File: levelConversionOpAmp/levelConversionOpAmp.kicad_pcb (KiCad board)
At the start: 2 copper layers, 21 parts, among them J1 IN, J2 OUT, Q1 PN2222A, Q2 PN2222A, U1 TL082

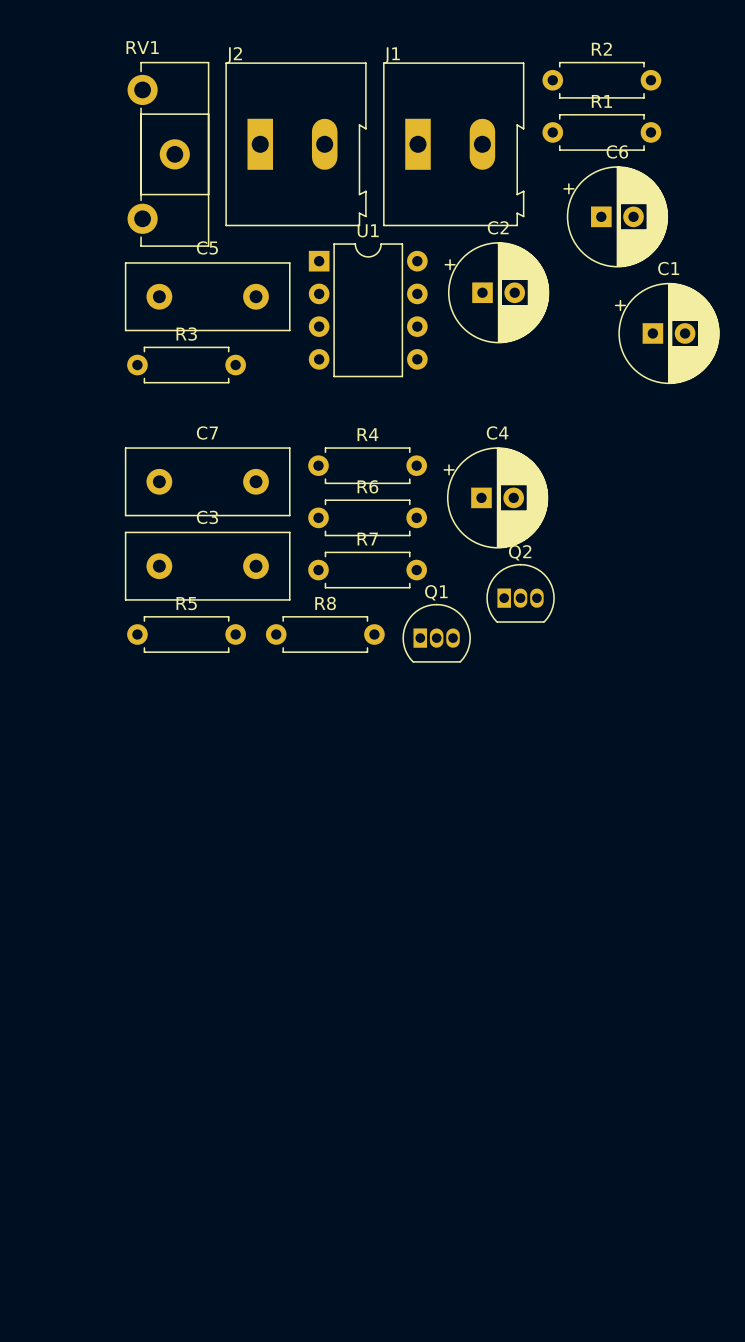
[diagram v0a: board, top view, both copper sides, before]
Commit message: Placement des composantes sur plaque perforee
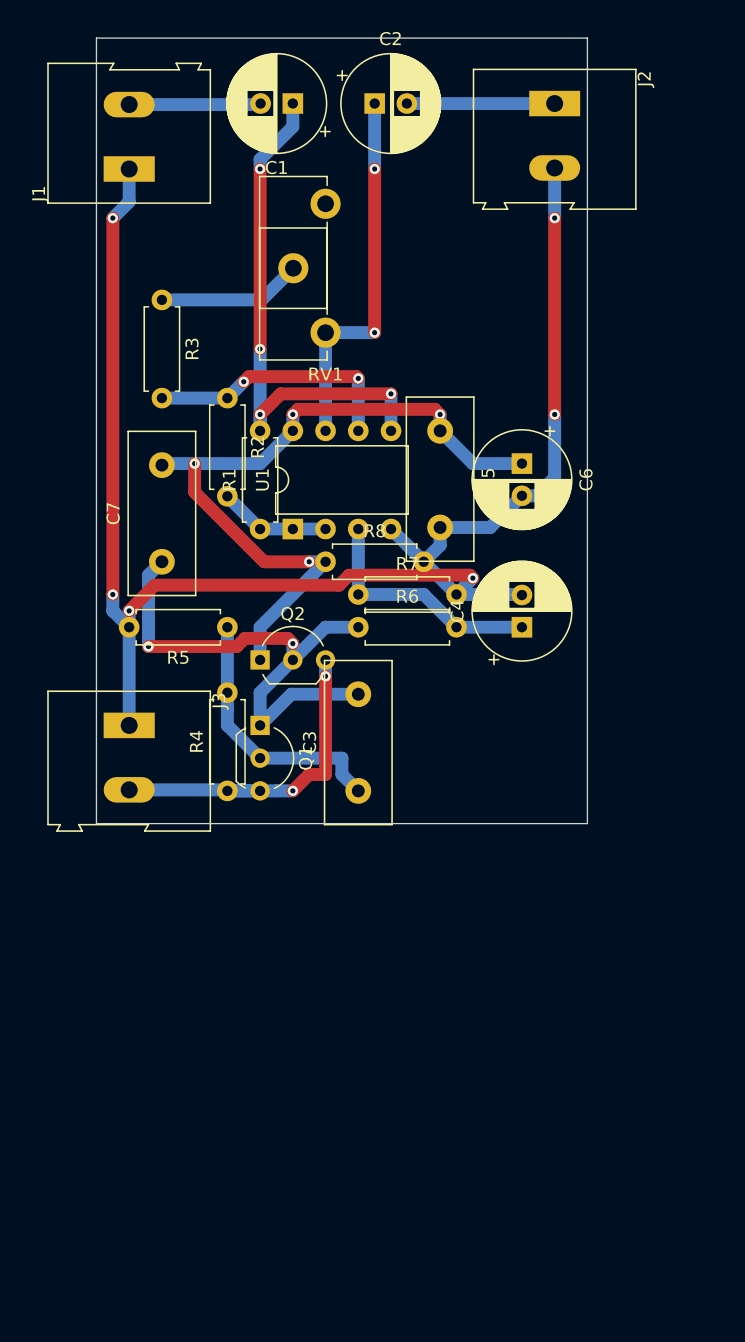
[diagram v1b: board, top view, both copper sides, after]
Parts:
- added J3: POW, TerminalBlock:TerminalBlock_Altech_AK300-2_P5.00mm, F.Cu at (129.5, 101.6)
- Q1, Q2: footprint Package_TO_SOT_THT:TO-92_Inline -> Package_TO_SOT_THT:TO-92_Inline_Wide
- moved R1 38.2 mm to (139.7, 86.4), turned to 90 degrees
- moved R2 35.3 mm to (137.2, 76.2), turned to 270 degrees
- moved C1 33.2 mm to (142.2, 53.3), turned to 180 degrees
- moved R4 26.2 mm to (137.2, 106.7), turned to 90 degrees
- moved C5 24.1 mm to (153.7, 78.7), turned to 270 degrees
- moved RV1 23.6 mm to (144.8, 71.1), turned to 180 degrees
- moved C3 23.3 mm to (147.3, 106.7), turned to 90 degrees
- moved J2 23.1 mm to (162.6, 53.3), turned to 270 degrees
- moved J1 22.5 mm to (129.5, 58.4), turned to 90 degrees
- moved U1 20.9 mm to (142.2, 86.4), turned to 90 degrees
- moved C6 20.1 mm to (160.0, 81.3), turned to 270 degrees
- moved Q2 19.5 mm to (139.7, 96.5)
- moved C2 16.9 mm to (148.6, 53.3)
- moved Q1 14.2 mm to (139.7, 101.6), turned to 270 degrees
- moved C4 10.5 mm to (160.0, 94.0), turned to 90 degrees
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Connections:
- J2 pad 1: GND -> SIGOUT
- J2 pad 2: SIGOUT -> GND
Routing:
- net GND: track 0.00 -> 125.2 mm, vias 0 -> 6
- net V+: track 0.00 -> 57.3 mm, vias 0 -> 4
- net Net-(C1-Pad1): track 0.00 -> 41.4 mm, vias 0 -> 4
- net Net-(C3-Pad2): track 0.00 -> 40.8 mm, vias 0 -> 2
- net Net-(C2-Pad1): track 0.00 -> 29.2 mm, vias 0 -> 2
- net +48V: track 0.00 -> 27.2 mm, vias 0 -> 2
- net Net-(C3-Pad1): track 0.00 -> 20.6 mm
- net Net-(R2-Pad1): track 0.00 -> 20.1 mm, vias 0 -> 2
- net Net-(C4-Pad1): track 0.00 -> 18.8 mm
- net SIGOUT: track 0.00 -> 11.5 mm
- net Net-(R3-Pad1): track 0.00 -> 11.2 mm
- net SIGIN: track 0.00 -> 10.2 mm
- net VREF: track 0.00 -> 8.67 mm
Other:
- board outline added: 38.1 x 61 mm

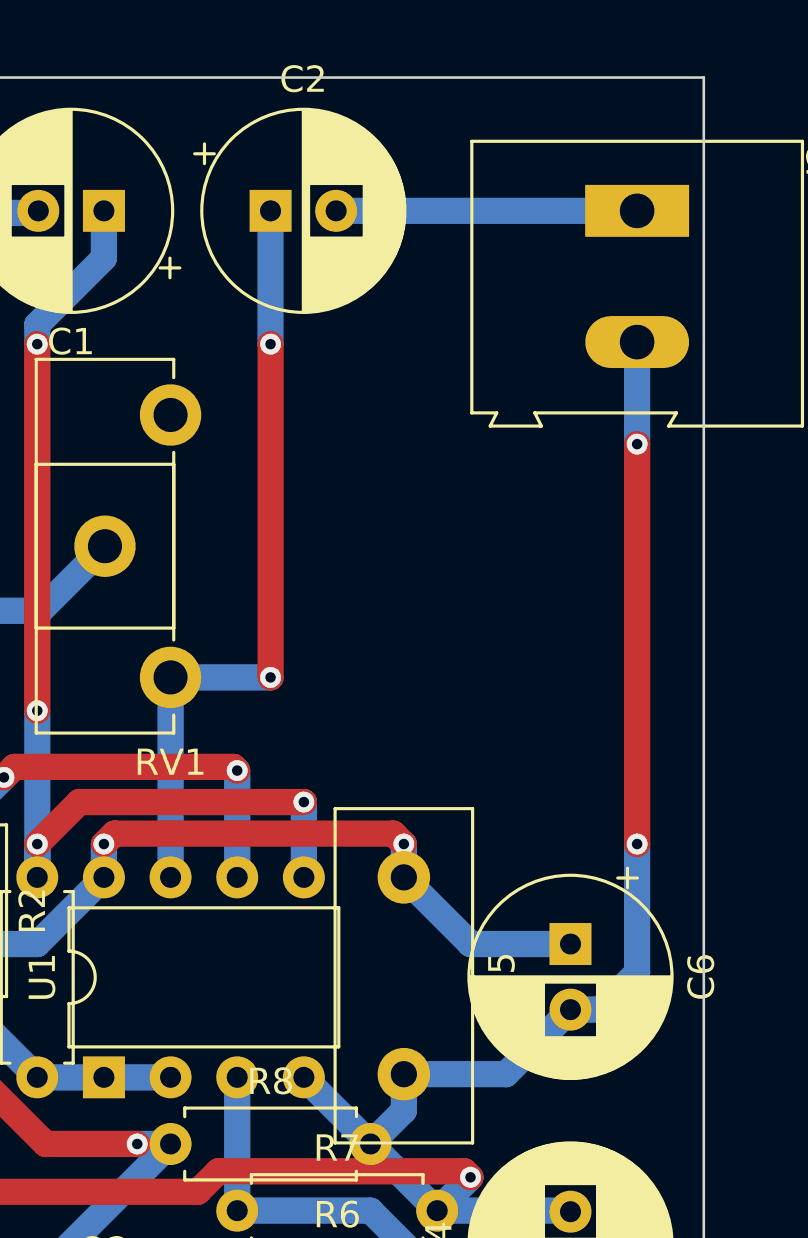
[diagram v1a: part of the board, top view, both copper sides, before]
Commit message: Changed layout a little. Added ground bias resistor at output to quickly set output DC level even when plugged into a high impedance load
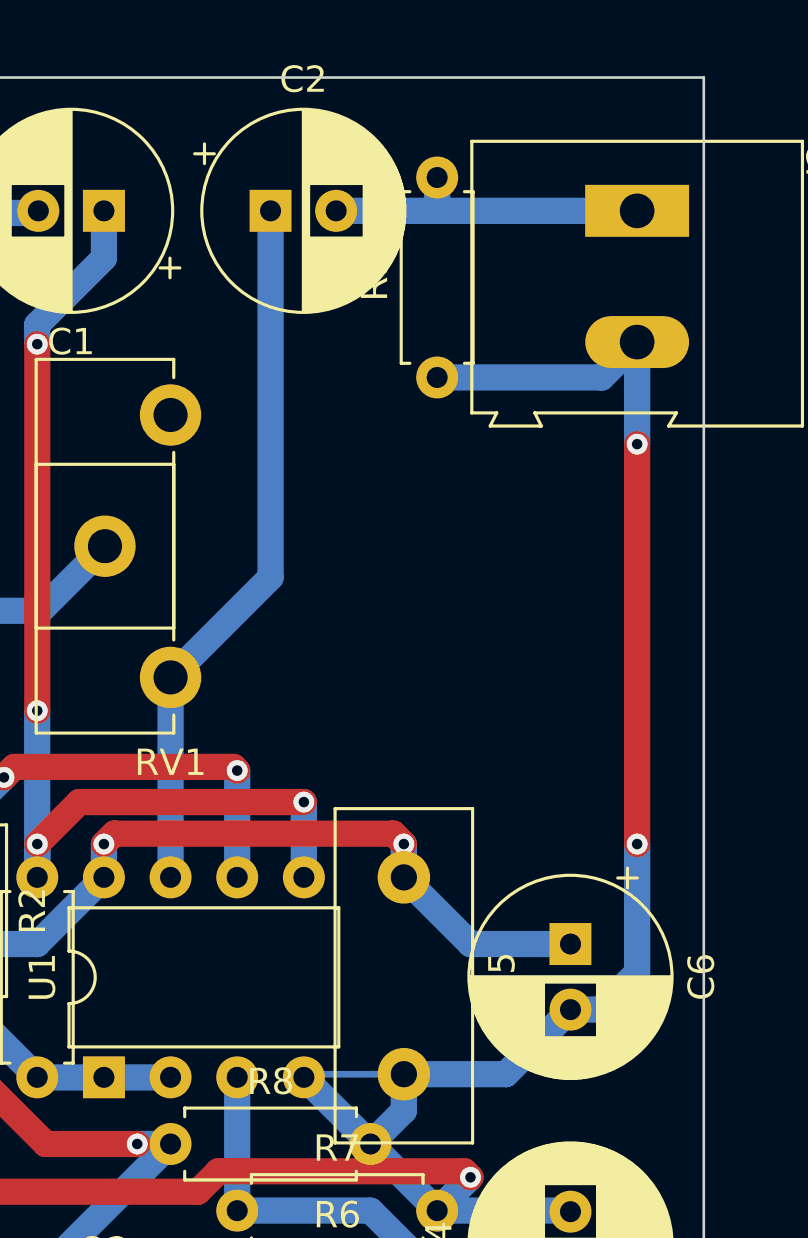
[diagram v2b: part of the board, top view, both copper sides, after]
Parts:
- added R9: 4k7, Resistor_THT:R_Axial_DIN0207_L6.3mm_D2.5mm_P7.62mm_Horizontal, F.Cu at (154.9, 59.7)
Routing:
- net GND: track 125.2 -> 137.2 mm
- net Net-(C2-Pad1): track 29.2 -> 27.0 mm, vias 2 -> 0
- net SIGOUT: track 11.5 -> 12.7 mm
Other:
- net class Default: via_dia 0.8 -> 0.5; via_drill 0.4 -> 0.3
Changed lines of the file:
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@@
     (thickness 1.6)
     (drawings 4)
-    (tracks 125)
+    (tracks 128)
     (zones 0)
-    (modules 22)
+    (modules 23)
     (nets 14)
   )
@@
   (setup
     (last_trace_width 1)
+    (user_trace_width 0.5)
     (user_trace_width 1)
     (trace_clearance 0.2)
@@
     (zone_45_only no)
     (trace_min 0.2)
-    (via_size 0.8)
-    (via_drill 0.4)
+    (via_size 0.5)
+    (via_drill 0.3)
     (via_min_size 0.4)
     (via_min_drill 0.3)
@@
     (clearance 0.2)
     (trace_width 0.25)
-    (via_dia 0.8)
-    (via_drill 0.4)
+    (via_dia 0.5)
+    (via_drill 0.3)
     (uvia_dia 0.3)
     (uvia_drill 0.1)
@@
     (add_net V+)
     (add_net VREF)
+  )
+  (module Resistor_THT:R_Axial_DIN0207_L6.3mm_D2.5mm_P7.62mm_Horizontal (layer F.Cu)
+    (at 154.94 59.69 90)
+    (descr "Resistor, Axial_DIN0207 series, Axial, Horizontal, pin pitch=7.62mm, 0.25W = 1/4W, length*diameter=6.3*2.5mm^2, http://cdn-reichelt.de/documents/datenblatt/B400/1_4W%23YAG.pdf")
+    (tags "Resistor Axial_DIN0207 series Axial Horizontal pin pitch 7.62mm 0.25W = 1/4W length 6.3mm diameter 2.5mm")
+    (fp_text reference R9 (at 3.81 -2.37 90) (layer F.SilkS)
+      (effects (font (size 1 1) (thickness 0.15)))
+    )
+    (fp_text value 4k7 (at 3.81 2.37 90) (layer F.Fab)
+      (effects (font (size 1 1) (thickness 0.15)))
+    )
+    (fp_text user %R (at 3.81 0 90) (layer F.Fab)
+      (effects (font (size 1 1) (thickness 0.15)))
+    )
+    (fp_line (start 8.67 -1.5) (end -1.05 -1.5) (layer F.CrtYd) (width 0.05))
+    (fp_line (start 8.67 1.5) (end 8.67 -1.5) (layer F.CrtYd) (width 0.05))
+    (fp_line (start -1.05 1.5) (end 8.67 1.5) (layer F.CrtYd) (width 0.05))
+    (fp_line (start -1.05 -1.5) (end -1.05 1.5) (layer F.CrtYd) (width 0.05))
+    (fp_line (start 7.08 1.37) (end 7.08 1.04) (layer F.SilkS) (width 0.12))
+    (fp_line (start 0.54 1.37) (end 7.08 1.37) (layer F.SilkS) (width 0.12))
+    (fp_line (start 0.54 1.04) (end 0.54 1.37) (layer F.SilkS) (width 0.12))
+    (fp_line (start 7.08 -1.37) (end 7.08 -1.04) (layer F.SilkS) (width 0.12))
+    (fp_line (start 0.54 -1.37) (end 7.08 -1.37) (layer F.SilkS) (width 0.12))
+    (fp_line (start 0.54 -1.04) (end 0.54 -1.37) (layer F.SilkS) (width 0.12))
+    (fp_line (start 7.62 0) (end 6.96 0) (layer F.Fab) (width 0.1))
+    (fp_line (start 0 0) (end 0.66 0) (layer F.Fab) (width 0.1))
+    (fp_line (start 6.96 -1.25) (end 0.66 -1.25) (layer F.Fab) (width 0.1))
+    (fp_line (start 6.96 1.25) (end 6.96 -1.25) (layer F.Fab) (width 0.1))
+    (fp_line (start 0.66 1.25) (end 6.96 1.25) (layer F.Fab) (width 0.1))
+    (fp_line (start 0.66 -1.25) (end 0.66 1.25) (layer F.Fab) (width 0.1))
+    (pad 2 thru_hole oval (at 7.62 0 90) (size 1.6 1.6) (drill 0.8) (layers *.Cu *.Mask)
+      (net 3 SIGOUT))
+    (pad 1 thru_hole circle (at 0 0 90) (size 1.6 1.6) (drill 0.8) (layers *.Cu *.Mask)
+      (net 7 GND))
+    (model ${KISYS3DMOD}/Resistor_THT.3dshapes/R_Axial_DIN0207_L6.3mm_D2.5mm_P7.62mm_Horizontal.wrl
+      (at (xyz 0 0 0))
+      (scale (xyz 1 1 1))
+      (rotate (xyz 0 0 0))
+    )
   )
   (module Potentiometer_THT:Potentiometer_ACP_CA14-H2,5_Horizontal (layer F.Cu)
@@
   (segment (start 139.66 53.42) (end 139.74 53.34) (width 1) (layer B.Cu) (net 1))
   (segment (start 129.54 53.42) (end 139.66 53.42) (width 1) (layer B.Cu) (net 1))
-  (via (at 139.7 77.47) (size 0.8) (drill 0.4) (layers F.Cu B.Cu) (net 2))
-  (segment (start 139.7 78.74) (end 139.7 77.47) (width 1) (layer B.Cu) (net 2))
-  (segment (start 141.300009 75.869991) (end 149.86 75.869991) (width 1) (layer F.Cu) (net 2))
-  (segment (start 139.7 77.47) (end 141.300009 75.869991) (width 1) (layer F.Cu) (net 2))
-  (via (at 149.86 75.869991) (size 0.8) (drill 0.4) (layers F.Cu B.Cu) (net 2))
-  (segment (start 149.86 75.869991) (end 149.86 78.74) (width 1) (layer B.Cu) (net 2))
   (segment (start 142.24 55.14) (end 139.7 57.68) (width 1) (layer B.Cu) (net 2))
   (segment (start 142.24 53.34) (end 142.24 55.14) (width 1) (layer B.Cu) (net 2))
@@
   (via (at 139.7 72.39) (size 0.8) (drill 0.4) (layers F.Cu B.Cu) (net 2))
   (segment (start 139.7 58.42) (end 139.7 72.39) (width 1) (layer F.Cu) (net 2))
+  (segment (start 139.7 78.74) (end 139.7 77.47) (width 1) (layer B.Cu) (net 2))
   (segment (start 139.7 72.39) (end 139.7 78.74) (width 1) (layer B.Cu) (net 2))
-  (segment (start 151.09 53.34) (end 162.56 53.34) (width 1) (layer B.Cu) (net 3))
-  (via (at 148.59 71.12) (size 0.8) (drill 0.4) (layers F.Cu B.Cu) (net 4))
-  (via (at 148.59 58.42) (size 0.8) (drill 0.4) (layers F.Cu B.Cu) (net 4))
-  (segment (start 148.59 71.12) (end 148.59 58.42) (width 1) (layer F.Cu) (net 4))
-  (segment (start 148.59 58.42) (end 148.59 53.34) (width 1) (layer B.Cu) (net 4))
-  (segment (start 144.78 71.12) (end 148.59 71.12) (width 1) (layer B.Cu) (net 4))
+  (segment (start 149.86 75.869991) (end 149.86 78.74) (width 1) (layer B.Cu) (net 2))
+  (via (at 149.86 75.869991) (size 0.8) (drill 0.4) (layers F.Cu B.Cu) (net 2))
+  (segment (start 141.300009 75.869991) (end 149.86 75.869991) (width 1) (layer F.Cu) (net 2))
+  (via (at 139.7 77.47) (size 0.8) (drill 0.4) (layers F.Cu B.Cu) (net 2))
+  (segment (start 139.7 77.47) (end 141.300009 75.869991) (width 1) (layer F.Cu) (net 2))
+  (segment (start 154.94 52.07) (end 154.94 53.34) (width 1) (layer B.Cu) (net 3))
+  (segment (start 154.94 53.34) (end 162.56 53.34) (width 1) (layer B.Cu) (net 3))
+  (segment (start 151.09 53.34) (end 154.94 53.34) (width 1) (layer B.Cu) (net 3))
   (segment (start 144.78 71.12) (end 144.78 78.74) (width 1) (layer B.Cu) (net 4))
+  (segment (start 148.59 67.31) (end 144.78 71.12) (width 1) (layer B.Cu) (net 4))
+  (segment (start 148.59 53.34) (end 148.59 67.31) (width 1) (layer B.Cu) (net 4))
   (segment (start 144.78 93.98) (end 142.24 96.52) (width 1) (layer B.Cu) (net 5))
   (segment (start 147.32 93.98) (end 144.78 93.98) (width 1) (layer B.Cu) (net 5))
@@
   (segment (start 162.56 82.37137) (end 161.15137 83.78) (width 1) (layer B.Cu) (net 7))
   (segment (start 162.56 77.47) (end 162.56 82.37137) (width 1) (layer B.Cu) (net 7))
+  (segment (start 149.98 86.24) (end 149.86 86.36) (width 0.25) (layer B.Cu) (net 7))
+  (segment (start 153.67 86.24) (end 149.98 86.24) (width 0.25) (layer B.Cu) (net 7))
+  (segment (start 161.21 59.69) (end 162.56 58.34) (width 1) (layer B.Cu) (net 7))
+  (segment (start 154.94 59.69) (end 161.21 59.69) (width 1) (layer B.Cu) (net 7))
   (segment (start 152.4 91.44) (end 154.94 93.98) (width 1) (layer B.Cu) (net 8))
   (segment (start 147.32 91.44) (end 152.4 91.44) (width 1) (layer B.Cu) (net 8))
@@
   (segment (start 132.2 81.28) (end 132.08 81.4) (width 1) (layer B.Cu) (net 9))
   (segment (start 134.62 81.28) (end 132.2 81.28) (width 1) (layer B.Cu) (net 9))
-  (segment (start 139.7 81.28) (end 142.24 78.74) (width 1) (layer B.Cu) (net 9))
-  (segment (start 134.62 81.28) (end 139.7 81.28) (width 1) (layer B.Cu) (net 9))
   (segment (start 156.21 81.28) (end 153.67 78.74) (width 1) (layer B.Cu) (net 9))
   (segment (start 160.02 81.28) (end 156.21 81.28) (width 1) (layer B.Cu) (net 9))
@@
   (segment (start 153.67 77.47) (end 153.270001 77.070001) (width 1) (layer F.Cu) (net 9))
   (segment (start 142.24 77.47) (end 142.24 78.74) (width 1) (layer B.Cu) (net 9))
+  (segment (start 139.7 81.28) (end 142.24 78.74) (width 1) (layer B.Cu) (net 9))
+  (segment (start 134.62 81.28) (end 139.7 81.28) (width 1) (layer B.Cu) (net 9))
   (segment (start 137.08 106.6) (end 137.16 106.68) (width 1) (layer B.Cu) (net 10))
   (segment (start 129.54 106.6) (end 137.08 106.6) (width 1) (layer B.Cu) (net 10))
@@
   (segment (start 142.24 86.36) (end 144.78 86.36) (width 1) (layer B.Cu) (net 11))
   (segment (start 132.08 76.2) (end 137.16 76.2) (width 1) (layer B.Cu) (net 12))
+  (segment (start 147.32 74.669981) (end 147.32 78.74) (width 1) (layer B.Cu) (net 12))
+  (segment (start 147.18002 74.530001) (end 147.32 74.669981) (width 1) (layer F.Cu) (net 12))
+  (via (at 147.32 74.669981) (size 0.8) (drill 0.4) (layers F.Cu B.Cu) (net 12))
+  (segment (start 138.829999 74.530001) (end 147.18002 74.530001) (width 1) (layer F.Cu) (net 12))
+  (segment (start 137.16 76.2) (end 138.43 74.93) (width 1) (layer B.Cu) (net 12))
   (via (at 138.43 74.93) (size 0.8) (drill 0.4) (layers F.Cu B.Cu) (net 12))
-  (segment (start 137.16 76.2) (end 138.43 74.93) (width 1) (layer B.Cu) (net 12))
-  (segment (start 147.18002 74.530001) (end 147.32 74.669981) (width 1) (layer F.Cu) (net 12))
-  (segment (start 138.829999 74.530001) (end 147.18002 74.530001) (width 1) (layer F.Cu) (net 12))
   (segment (start 138.43 74.93) (end 138.829999 74.530001) (width 1) (layer F.Cu) (net 12))
-  (via (at 147.32 74.669981) (size 0.8) (drill 0.4) (layers F.Cu B.Cu) (net 12))
-  (segment (start 147.32 74.669981) (end 147.32 78.74) (width 1) (layer B.Cu) (net 12))
   (segment (start 139.82 68.58) (end 142.28 66.12) (width 1) (layer B.Cu) (net 13))
   (segment (start 132.08 68.58) (end 139.82 68.58) (width 1) (layer B.Cu) (net 13))
